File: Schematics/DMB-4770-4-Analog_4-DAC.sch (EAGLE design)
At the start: 58 parts, among them IC1 LMV344, IC2 OPA4743UA, U1 MCP4728-E/UN, X1 1751316, X2 1751316

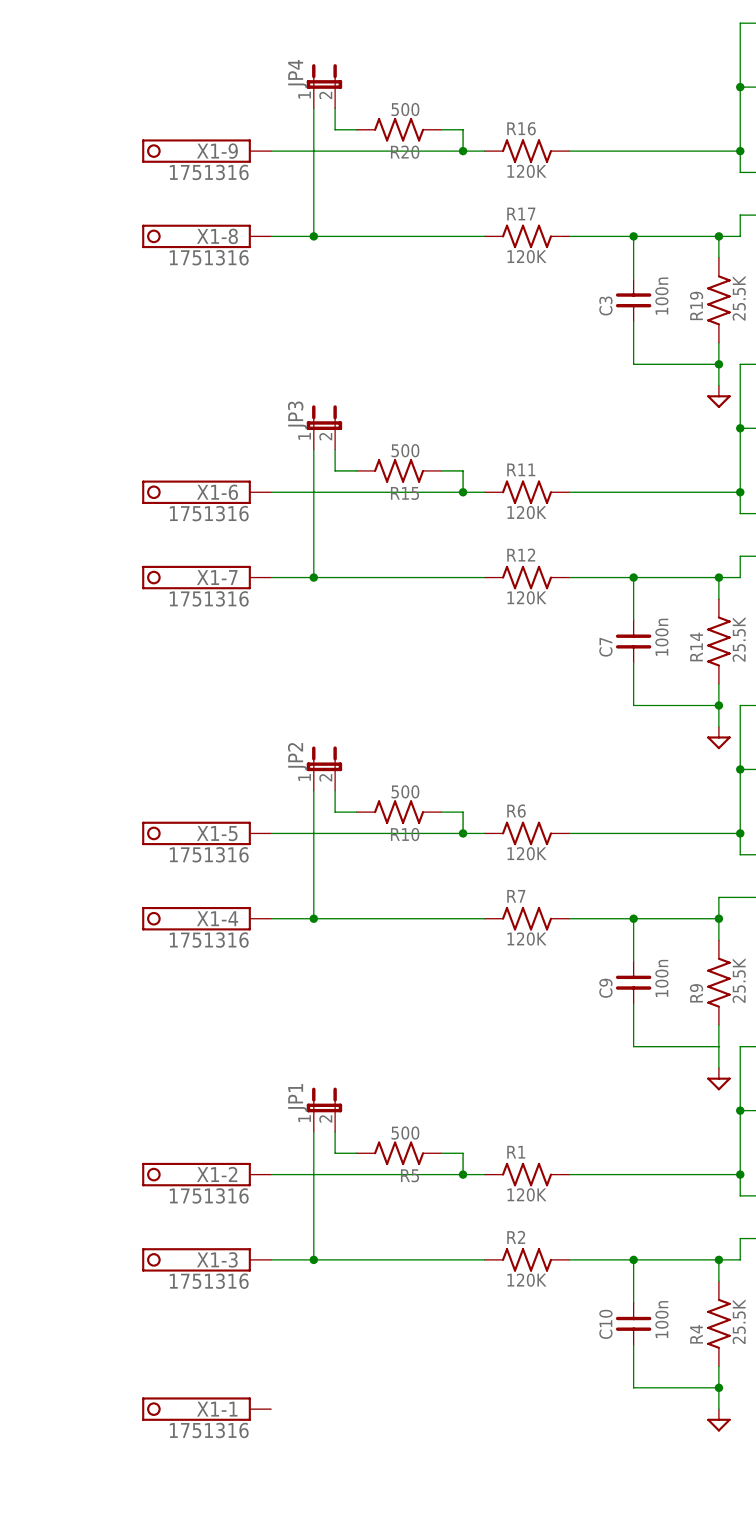
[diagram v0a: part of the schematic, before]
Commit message: Correction schémas pour ajout des diodes de protection
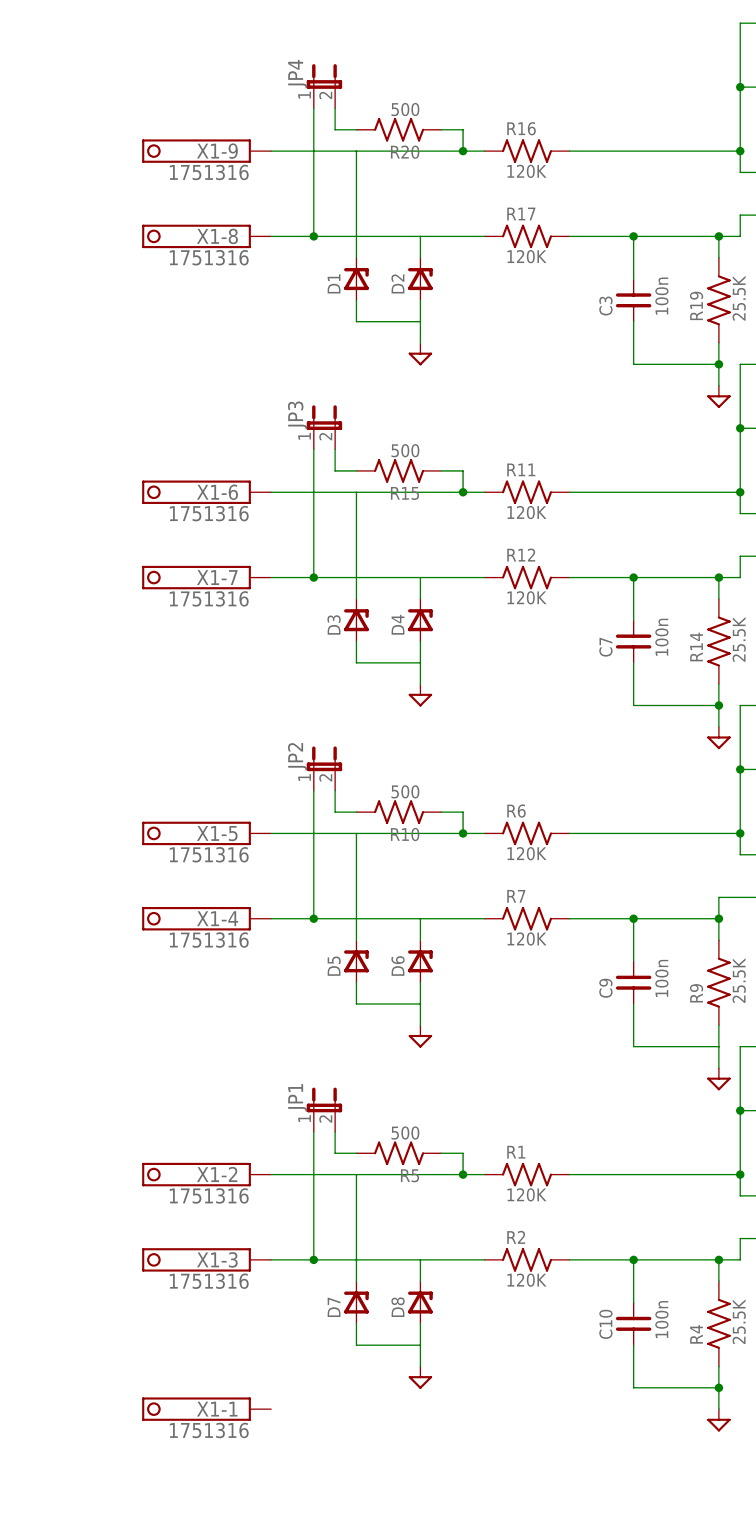
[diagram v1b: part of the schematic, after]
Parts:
- added D1, D2, D3, D4, D5, D6, D7, D8: (no value), diodes:DZS
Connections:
- new net N$33: D4.C
- new net N$37: D3.C
- new net N$40: D6.C
- new net N$42: D5.C
- new net N$49: D8.C
- new net N$50: D7.C
- net DGND: now also D1.A, D2.A, D3.A, D4.A, D5.A, D6.A, D7.A, D8.A
- net N$22: now also D2.C
- net N$24: now also D1.C
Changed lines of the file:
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@@
 <part name="$22" library="signals" deviceset="VDG" device=""/>
 <part name="$23" library="signals" deviceset="V+12V" device=""/>
+<part name="D1" library="diodes" deviceset="DZ" device="S"/>
+<part name="D2" library="diodes" deviceset="DZ" device="S"/>
+<part name="$24" library="signals" deviceset="VDG" device=""/>
+<part name="D3" library="diodes" deviceset="DZ" device="S"/>
+<part name="D4" library="diodes" deviceset="DZ" device="S"/>
+<part name="$25" library="signals" deviceset="VDG" device=""/>
+<part name="D5" library="diodes" deviceset="DZ" device="S"/>
+<part name="D6" library="diodes" deviceset="DZ" device="S"/>
+<part name="$26" library="signals" deviceset="VDG" device=""/>
+<part name="D7" library="diodes" deviceset="DZ" device="S"/>
+<part name="D8" library="diodes" deviceset="DZ" device="S"/>
+<part name="$27" library="signals" deviceset="VDG" device=""/>
 </parts>
 <sheets>
@@
 <instance part="$22" gate="G$1" x="198.12" y="30.48"/>
 <instance part="$23" gate="G$1" x="330.2" y="243.84"/>
+<instance part="D1" gate="G$1" x="63.5" y="172.72" rot="R90"/>
+<instance part="D2" gate="G$1" x="71.12" y="172.72" rot="R90"/>
+<instance part="$24" gate="G$1" x="71.12" y="165.1"/>
+<instance part="D3" gate="G$1" x="63.5" y="132.08" rot="R90"/>
+<instance part="D4" gate="G$1" x="71.12" y="132.08" rot="R90"/>
+<instance part="$25" gate="G$1" x="71.12" y="124.46"/>
+<instance part="D5" gate="G$1" x="63.5" y="91.44" rot="R90"/>
+<instance part="D6" gate="G$1" x="71.12" y="91.44" rot="R90"/>
+<instance part="$26" gate="G$1" x="71.12" y="83.82"/>
+<instance part="D7" gate="G$1" x="63.5" y="50.8" rot="R90"/>
+<instance part="D8" gate="G$1" x="71.12" y="50.8" rot="R90"/>
+<instance part="$27" gate="G$1" x="71.12" y="43.18"/>
 </instances>
 <busses>
@@
 <wire x1="198.12" y1="35.56" x2="198.12" y2="30.48" width="0.1524" layer="91"/>
 </segment>
+<segment>
+<pinref part="D1" gate="G$1" pin="A"/>
+<wire x1="63.5" y1="170.18" x2="63.5" y2="167.64" width="0.1524" layer="91"/>
+<wire x1="63.5" y1="167.64" x2="71.12" y2="167.64" width="0.1524" layer="91"/>
+<pinref part="$24" gate="G$1" pin="DGND"/>
+<wire x1="71.12" y1="167.64" x2="71.12" y2="165.1" width="0.1524" layer="91"/>
+<pinref part="D2" gate="G$1" pin="A"/>
+<wire x1="71.12" y1="167.64" x2="71.12" y2="170.18" width="0.1524" layer="91"/>
+</segment>
+<segment>
+<pinref part="D3" gate="G$1" pin="A"/>
+<wire x1="63.5" y1="129.54" x2="63.5" y2="127" width="0.1524" layer="91"/>
+<wire x1="63.5" y1="127" x2="71.12" y2="127" width="0.1524" layer="91"/>
+<pinref part="$25" gate="G$1" pin="DGND"/>
+<wire x1="71.12" y1="127" x2="71.12" y2="124.46" width="0.1524" layer="91"/>
+<pinref part="D4" gate="G$1" pin="A"/>
+<wire x1="71.12" y1="127" x2="71.12" y2="129.54" width="0.1524" layer="91"/>
+</segment>
+<segment>
+<pinref part="D5" gate="G$1" pin="A"/>
+<wire x1="63.5" y1="88.9" x2="63.5" y2="86.36" width="0.1524" layer="91"/>
+<wire x1="63.5" y1="86.36" x2="71.12" y2="86.36" width="0.1524" layer="91"/>
+<pinref part="$26" gate="G$1" pin="DGND"/>
+<wire x1="71.12" y1="86.36" x2="71.12" y2="83.82" width="0.1524" layer="91"/>
+<pinref part="D6" gate="G$1" pin="A"/>
+<wire x1="71.12" y1="86.36" x2="71.12" y2="88.9" width="0.1524" layer="91"/>
+</segment>
+<segment>
+<pinref part="D7" gate="G$1" pin="A"/>
+<wire x1="63.5" y1="48.26" x2="63.5" y2="45.72" width="0.1524" layer="91"/>
+<wire x1="63.5" y1="45.72" x2="71.12" y2="45.72" width="0.1524" layer="91"/>
+<pinref part="$27" gate="G$1" pin="DGND"/>
+<wire x1="71.12" y1="45.72" x2="71.12" y2="43.18" width="0.1524" layer="91"/>
+<pinref part="D8" gate="G$1" pin="A"/>
+<wire x1="71.12" y1="45.72" x2="71.12" y2="48.26" width="0.1524" layer="91"/>
+</segment>
 </net>
 <net name="N$5" class="0">
@@
 <segment>
 <pinref part="R17" gate="G$1" pin="1"/>
-<wire x1="78.74" y1="177.8" x2="58.42" y2="177.8" width="0.1524" layer="91"/>
+<wire x1="78.74" y1="177.8" x2="71.12" y2="177.8" width="0.1524" layer="91"/>
 <pinref part="JP4" gate="A" pin="1"/>
+<wire x1="71.12" y1="177.8" x2="58.42" y2="177.8" width="0.1524" layer="91"/>
 <wire x1="58.42" y1="193.04" x2="58.42" y2="177.8" width="0.1524" layer="91"/>
 <junction x="58.42" y="177.8"/>
 <pinref part="X1" gate="-8" pin="K"/>
 <wire x1="53.34" y1="177.8" x2="58.42" y2="177.8" width="0.1524" layer="91"/>
+<pinref part="D2" gate="G$1" pin="C"/>
+<wire x1="71.12" y1="175.26" x2="71.12" y2="177.8" width="0.1524" layer="91"/>
 </segment>
 </net>
@@
 <pinref part="R16" gate="G$1" pin="1"/>
 <wire x1="78.74" y1="187.96" x2="76.2" y2="187.96" width="0.1524" layer="91"/>
-<wire x1="76.2" y1="187.96" x2="53.34" y2="187.96" width="0.1524" layer="91"/>
+<wire x1="76.2" y1="187.96" x2="63.5" y2="187.96" width="0.1524" layer="91"/>
+<wire x1="63.5" y1="187.96" x2="53.34" y2="187.96" width="0.1524" layer="91"/>
 <wire x1="76.2" y1="190.5" x2="76.2" y2="187.96" width="0.1524" layer="91"/>
 <junction x="76.2" y="187.96"/>
 <pinref part="X1" gate="-9" pin="K"/>
+<pinref part="D1" gate="G$1" pin="C"/>
+<wire x1="63.5" y1="175.26" x2="63.5" y2="187.96" width="0.1524" layer="91"/>
 </segment>
 </net>
@@
 </segment>
 </net>
+<net name="N$33" class="0">
+<segment>
+<pinref part="D4" gate="G$1" pin="C"/>
+<wire x1="71.12" y1="134.62" x2="71.12" y2="137.16" width="0.1524" layer="91"/>
+</segment>
+</net>
+<net name="N$37" class="0">
+<segment>
+<pinref part="D3" gate="G$1" pin="C"/>
+<wire x1="63.5" y1="134.62" x2="63.5" y2="147.32" width="0.1524" layer="91"/>
+</segment>
+</net>
+<net name="N$40" class="0">
+<segment>
+<pinref part="D6" gate="G$1" pin="C"/>
+<wire x1="71.12" y1="93.98" x2="71.12" y2="96.52" width="0.1524" layer="91"/>
+</segment>
+</net>
+<net name="N$42" class="0">
+<segment>
+<pinref part="D5" gate="G$1" pin="C"/>
+<wire x1="63.5" y1="93.98" x2="63.5" y2="106.68" width="0.1524" layer="91"/>
+</segment>
+</net>
+<net name="N$49" class="0">
+<segment>
+<pinref part="D8" gate="G$1" pin="C"/>
+<wire x1="71.12" y1="53.34" x2="71.12" y2="55.88" width="0.1524" layer="91"/>
+</segment>
+</net>
+<net name="N$50" class="0">
+<segment>
+<pinref part="D7" gate="G$1" pin="C"/>
+<wire x1="63.5" y1="53.34" x2="63.5" y2="66.04" width="0.1524" layer="91"/>
+</segment>
+</net>

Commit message: Correction valeurs
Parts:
- R1, R11, R12, R16, R17, R2, R6, R7: value 120K -> 102K
- R23, R25, R27, R29: value 20K -> 82.5K
- R24, R26, R28, R30: value 80K -> 330K
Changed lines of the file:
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@@
 <parts>
 <part name="IC1" library="linear" deviceset="LMV324?*" device="M" value="LMV344"/>
-<part name="R1" library="divers" deviceset="RU" device="0805" value="120K"/>
-<part name="R2" library="divers" deviceset="RU" device="0805" value="120K"/>
+<part name="R1" library="divers" deviceset="RU" device="0805" value="102K"/>
+<part name="R2" library="divers" deviceset="RU" device="0805" value="102K"/>
 <part name="R3" library="divers" deviceset="RU" device="0805" value="25.5K"/>
 <part name="R4" library="divers" deviceset="RU" device="0805" value="25.5K"/>
@@
 <part name="X1" library="con-phoenix-350" deviceset="1751316" device=""/>
 <part name="$1" library="signals" deviceset="VDG" device=""/>
-<part name="R6" library="divers" deviceset="RU" device="0805" value="120K"/>
-<part name="R7" library="divers" deviceset="RU" device="0805" value="120K"/>
+<part name="R6" library="divers" deviceset="RU" device="0805" value="102K"/>
+<part name="R7" library="divers" deviceset="RU" device="0805" value="102K"/>
 <part name="R8" library="divers" deviceset="RU" device="0805" value="25.5K"/>
 <part name="R9" library="divers" deviceset="RU" device="0805" value="25.5K"/>
@@
 <part name="JP2" library="jumper" deviceset="JP1E" device=""/>
 <part name="$2" library="signals" deviceset="VDG" device=""/>
-<part name="R11" library="divers" deviceset="RU" device="0805" value="120K"/>
-<part name="R12" library="divers" deviceset="RU" device="0805" value="120K"/>
+<part name="R11" library="divers" deviceset="RU" device="0805" value="102K"/>
+<part name="R12" library="divers" deviceset="RU" device="0805" value="102K"/>
 <part name="R13" library="divers" deviceset="RU" device="0805" value="25.5K"/>
 <part name="R14" library="divers" deviceset="RU" device="0805" value="25.5K"/>
@@
 <part name="JP3" library="jumper" deviceset="JP1E" device=""/>
 <part name="$3" library="signals" deviceset="VDG" device=""/>
-<part name="R16" library="divers" deviceset="RU" device="0805" value="120K"/>
-<part name="R17" library="divers" deviceset="RU" device="0805" value="120K"/>
+<part name="R16" library="divers" deviceset="RU" device="0805" value="102K"/>
+<part name="R17" library="divers" deviceset="RU" device="0805" value="102K"/>
 <part name="R18" library="divers" deviceset="RU" device="0805" value="25.5K"/>
 <part name="R19" library="divers" deviceset="RU" device="0805" value="25.5K"/>
@@
 <part name="$11" library="signals" deviceset="V+3V3" device=""/>
 <part name="$12" library="signals" deviceset="VDG" device=""/>
-<part name="R23" library="divers" deviceset="RU" device="0805" value="20K"/>
-<part name="R24" library="divers" deviceset="RU" device="0805" value="80K"/>
-<part name="R25" library="divers" deviceset="RU" device="0805" value="20K"/>
-<part name="R26" library="divers" deviceset="RU" device="0805" value="80K"/>
-<part name="R27" library="divers" deviceset="RU" device="0805" value="20K"/>
-<part name="R28" library="divers" deviceset="RU" device="0805" value="80K"/>
-<part name="R29" library="divers" deviceset="RU" device="0805" value="20K"/>
-<part name="R30" library="divers" deviceset="RU" device="0805" value="80K"/>
+<part name="R23" library="divers" deviceset="RU" device="0805" value="82.5K"/>
+<part name="R24" library="divers" deviceset="RU" device="0805" value="330K"/>
+<part name="R25" library="divers" deviceset="RU" device="0805" value="82.5K"/>
+<part name="R26" library="divers" deviceset="RU" device="0805" value="330K"/>
+<part name="R27" library="divers" deviceset="RU" device="0805" value="82.5K"/>
+<part name="R28" library="divers" deviceset="RU" device="0805" value="330K"/>
+<part name="R29" library="divers" deviceset="RU" device="0805" value="82.5K"/>
+<part name="R30" library="divers" deviceset="RU" device="0805" value="330K"/>
 <part name="X2" library="con-phoenix-350" deviceset="1751316" device=""/>
 <part name="$13" library="signals" deviceset="VDG" device=""/>

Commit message: Modification empreintes resistances
Au lieu de 2 resistances 500, une seule 250 en 1206
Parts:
- R10, R20, R5: value 500 -> 250
- R15: value 500 -> 150
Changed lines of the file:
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@@
 <part name="R3" library="divers" deviceset="RU" device="0805" value="25.5K"/>
 <part name="R4" library="divers" deviceset="RU" device="0805" value="25.5K"/>
-<part name="R5" library="divers" deviceset="RU" device="0805" value="500"/>
+<part name="R5" library="divers" deviceset="RU" device="0805" value="250"/>
 <part name="JP1" library="jumper" deviceset="JP1E" device=""/>
 <part name="X1" library="con-phoenix-350" deviceset="1751316" device=""/>
@@
 <part name="R8" library="divers" deviceset="RU" device="0805" value="25.5K"/>
 <part name="R9" library="divers" deviceset="RU" device="0805" value="25.5K"/>
-<part name="R10" library="divers" deviceset="RU" device="0805" value="500"/>
+<part name="R10" library="divers" deviceset="RU" device="0805" value="250"/>
 <part name="JP2" library="jumper" deviceset="JP1E" device=""/>
 <part name="$2" library="signals" deviceset="VDG" device=""/>
@@
 <part name="R13" library="divers" deviceset="RU" device="0805" value="25.5K"/>
 <part name="R14" library="divers" deviceset="RU" device="0805" value="25.5K"/>
-<part name="R15" library="divers" deviceset="RU" device="0805" value="500"/>
+<part name="R15" library="divers" deviceset="RU" device="0805" value="150"/>
 <part name="JP3" library="jumper" deviceset="JP1E" device=""/>
 <part name="$3" library="signals" deviceset="VDG" device=""/>
@@
 <part name="R18" library="divers" deviceset="RU" device="0805" value="25.5K"/>
 <part name="R19" library="divers" deviceset="RU" device="0805" value="25.5K"/>
-<part name="R20" library="divers" deviceset="RU" device="0805" value="500"/>
+<part name="R20" library="divers" deviceset="RU" device="0805" value="250"/>
 <part name="JP4" library="jumper" deviceset="JP1E" device=""/>
 <part name="$4" library="signals" deviceset="VDG" device=""/>
